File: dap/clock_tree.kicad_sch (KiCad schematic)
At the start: 4 parts, among them U3 AD9515, U4 ADF4351, U5 SN74AUC74RGYR, U6 SN74AUC74RGYR

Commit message: general setup
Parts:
- added C41: 22u 16V, symbol Device:C_Polarized_Small
- added C42, C44, C62, C65: 1u, symbol Device:C_Small
- added C45: 100p, symbol Device:C_Small
- added C46, C47, C67, C68, C69, C70: 1n, symbol Device:C_Small
- added C48, C50, C52, C55, C57: 0.1u, symbol Device:C_Small
- added C49, C51, C53, C54, C56: 10p, symbol Device:C_Small
- added C58: 2700p, symbol Device:C_Small
- added C59: 39n, symbol Device:C_Small
- added C60: 1200p, symbol Device:C_Small
- added C61, C63, C64, C66: 120p, symbol Device:C_Small
- added D1: BZX84Cxx, Package_TO_SOT_SMD:SOT-23, symbol Diode:BZX84Cxx
- added D2: Red, symbol Device:LED_Small
- added D3: Green, symbol Device:LED_Small
- added J34: Alt RF-In, symbol Connector:Conn_01x02_Pin
- added J35: RPi, symbol Connector:Conn_01x01_Pin
- added L? (x4): 1.9n, symbol Device:L_Small
- added L?: Ferrite Beads, symbol Device:L_Ferrite_Small
- added L? (x4): 7.5n, symbol Device:L_Small
- added R16: 1k, symbol Device:R_Small_US
- added R17, R21, R25, R34, R35, R36, R37: 0, symbol Device:R_Small_US
- added R18, R19, R20, R22, R23: 10k, symbol Device:R_Small_US
- added R24: 51, symbol Device:R_Small_US
- added R26: 4.7k, symbol Device:R_Small_US
- added R27: DNI, symbol Device:R_Small_US
- added R28, R30, R31: R_Small_US, symbol Device:R_Small_US
- added R29: 100, symbol Device:R_Small_US
- added R32: 360, symbol Device:R_Small_US
- added R33: 680, symbol Device:R_Small_US
- added R38, R39, R40: 50, symbol Device:R_Small_US
- added TP1: AVDD, symbol Connector:TestPoint_Small
- added TP10: LD, symbol Connector:TestPoint_Small
- added TP11: MUXOUT, symbol Connector:TestPoint_Small
- added TP3: T1, symbol Connector:TestPoint_Small
- added TP4: CE, symbol Connector:TestPoint_Small
- added TP5: LE, symbol Connector:TestPoint_Small
- added TP6: DATA, symbol Connector:TestPoint_Small
- added TP7: PDRF, symbol Connector:TestPoint_Small
- added TP8: T2, symbol Connector:TestPoint_Small
- added TP9: CLK, symbol Connector:TestPoint_Small
- added U21: ADF4351BCPZ, hf-transceiver:CP-32-7_ADI, symbol hf-transceiver:ADF4351BCPZ
- added U9: ADP150ACBZ-3.3-R7, hf-transceiver:CB_4_3_ADI, symbol hf-transceiver:ADP150ACBZ-3.3-R7
- added Y?: 25MHz, symbol Device:Crystal_GND24_Small
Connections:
- new net: C56.2, C57.2, U21.19 (TEMP)
- new net: C54.2, C55.2, U21.23 (VCOM)
- new net: C44.1, C45.1, L?.1, Y?.1
- new net: D3.2 (A), R28.2, R29.2, R30.2, R31.1
- new net: C69.1, L?.2, R36.2
- new net: C69.2, L?.1
- new net: R34.1, U21.12 (RFOUTA+)
- new net: R35.1, U21.13 (RFOUTA-)
- new net: R36.1, U21.14 (RFOUTB+)
- new net: R37.1, U21.15 (RFOUTB-)
- new net: R26.2, U21.22 (RSET)
- new net: R29.1, TP10.1, U21.25 (LD)
- new net: R30.1, TP11.1, U21.30 (MUXOUT)
- new net: C58.2, C59.2, R33.1, U21.7 (CPOUT)
- new net: C70.1, L?.1, R37.2
- new net: C46.2, C47.1, R24.2
- new net: L?.2, R39.1
- new net: C46.1, J34.1 (Pin_1), R21.2, TP3.1
- new net: C59.1, R32.2
- new net: R21.1, Y?.3
- new net: C68.1, L?.1, R35.2
- new net: C70.2, L?.1
- new net: L?.2, R40.1
- new net: D2.2 (A), R16.2
- new net: C68.2, L?.1
- new net: C67.1, L?.2, R34.2
- new net: C67.2, L?.1
- new net +5: C41.1, C42.1, D1.3 (K), U9.A1 (VIN), U9.B1 (EN)
- new net AVDD: C48.1, C49.1, C50.1, C51.1, C52.1, C53.1, L?.2, R16.1, R17.2, R18.1, R19.1, R25.1, R28.1, TP1.1, U21.16 (VVCO), U21.17 (VVCO), U21.6 (VP), U9.A2 (VOUT)
- new net GND: C41.2, C42.2, C44.2, C45.2, C48.2, C49.2, C50.2, C51.2, C52.2, C53.2, C54.1, C55.1, C56.1, C57.1, C58.1, C60.1, C61.2, C62.2, C63.2, C64.2, C65.2, C66.2, D1.1 (A), D2.1 (K), D3.1 (K), J34.2 (Pin_2), R20.2, R22.2, R23.2, R24.1, R26.1, R27.2, R31.2, R32.1, R38.2, R39.2, R40.2, U9.B2 (GND), Y?.2, Y?.4
- new net LO-R: L?.2
- new net LO-T: L?.2, R38.1
- new net RPi-PDRF: J35.1 (Pin_1), R25.2, R27.1, TP7.1, U21.26 (PDBRF)
- new net SPI1_CE1: R18.2, TP4.1, U21.4 (CE)
- new net SPI1_MISO: R19.2, R23.1, TP5.1, U21.3 (LE)
- new net SPI1_MOSI: R22.1, TP6.1, U21.2 (DATA)
- new net SPI1_SCLK: R20.1, TP9.1, U21.1 (CLK)
- new net VOUT: C61.1, C62.1, C63.1, C64.1, C65.1, C66.1, L?.1, L?.1, L?.2, L?.2, R17.1
- new net VRef: C47.2, TP8.1, U21.29 (REFIN)
- new net VTune: C60.2, R33.2, U21.20 (VTUNE)
- no-connect marks 0 -> 1
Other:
- note added: "Lock Detect"
- moved on the sheet: U4

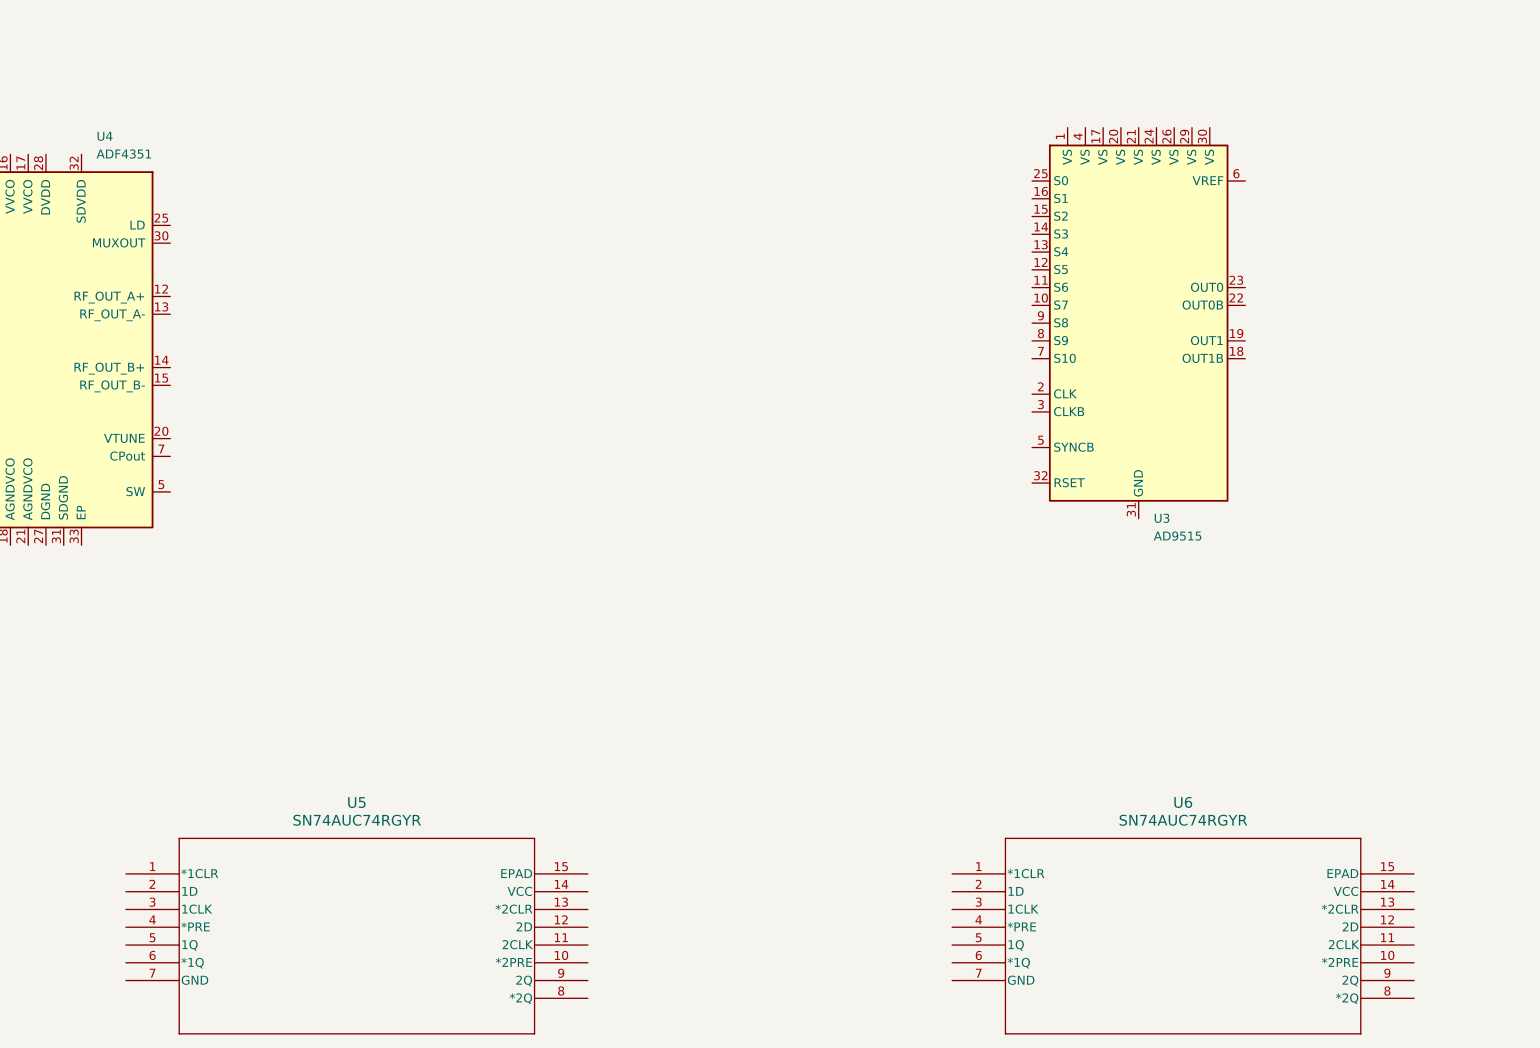
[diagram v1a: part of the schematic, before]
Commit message: selected clocking scheme
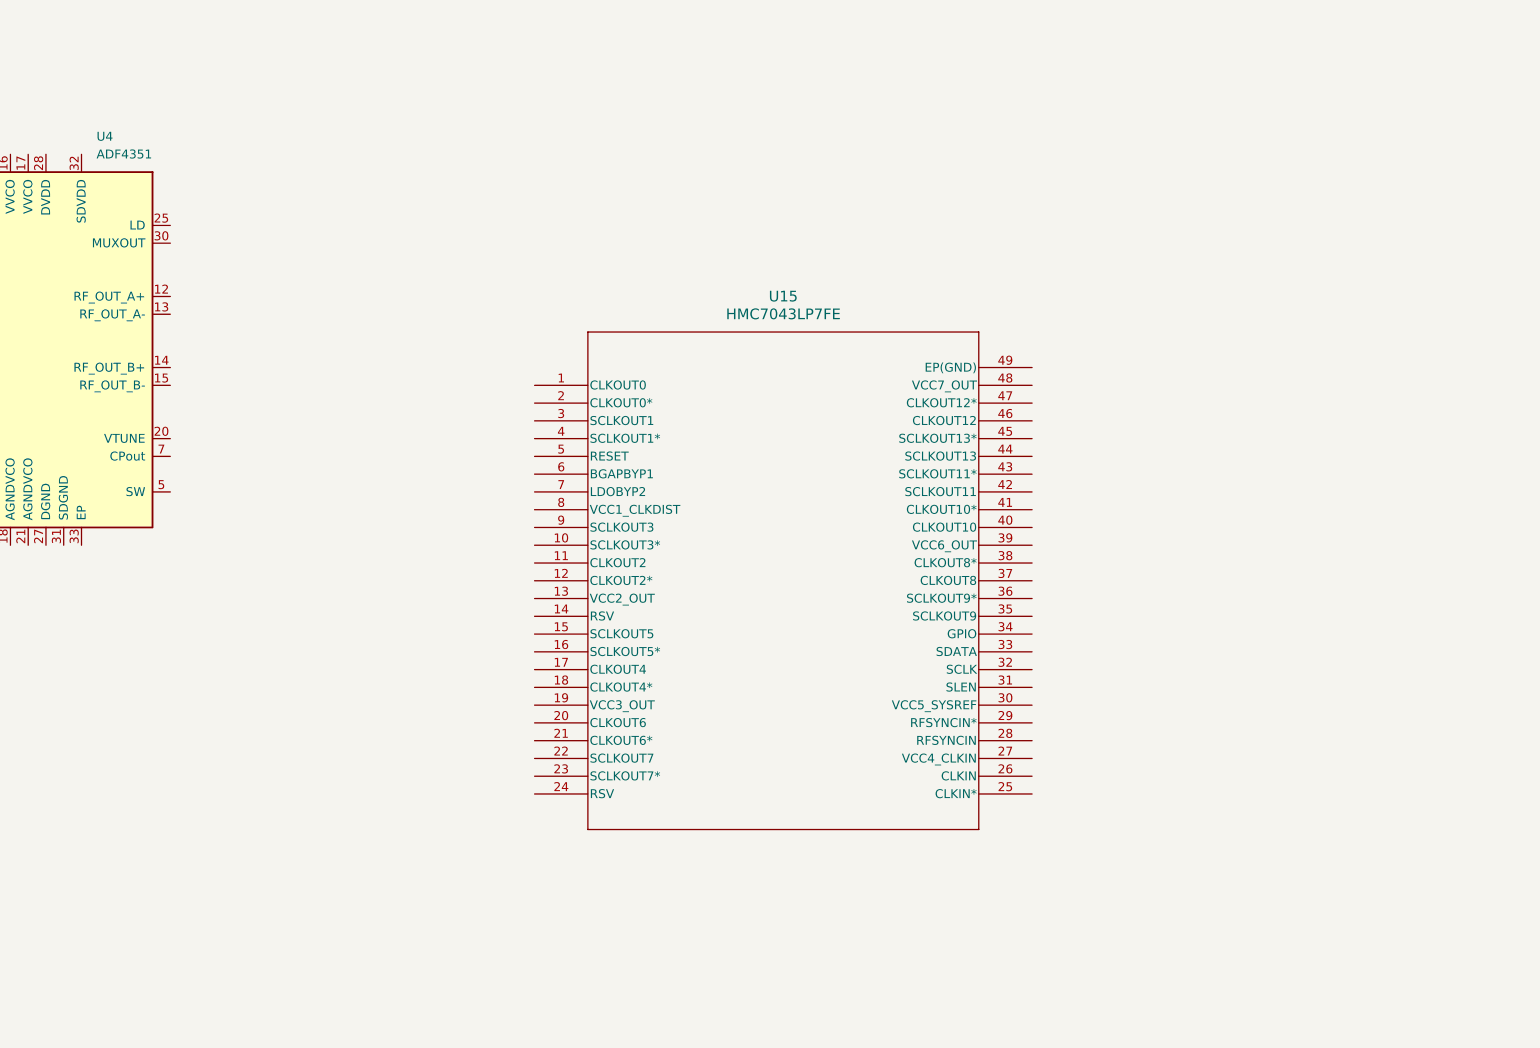
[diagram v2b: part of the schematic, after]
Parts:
- removed U3: AD9515, Package_CSP:LFCSP-32-1EP_5x5mm_P0.5mm_EP3.1x3.1mm, symbol Timer:AD9515
- removed U5, U6: SN74AUC74RGYR, RGY14_2P05X2P05, symbol SN74AUC74:SN74AUC74RGYR
- added U15: HMC7043LP7FE, HCP_48_1_ADI, symbol HMC7043:HMC7043LP7FE
